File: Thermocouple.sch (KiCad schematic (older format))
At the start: 25 parts, among them P2 CONN_3X2, P3 CONN_2, U2 MCP3901, U3 LMT84, U4 OPA4170

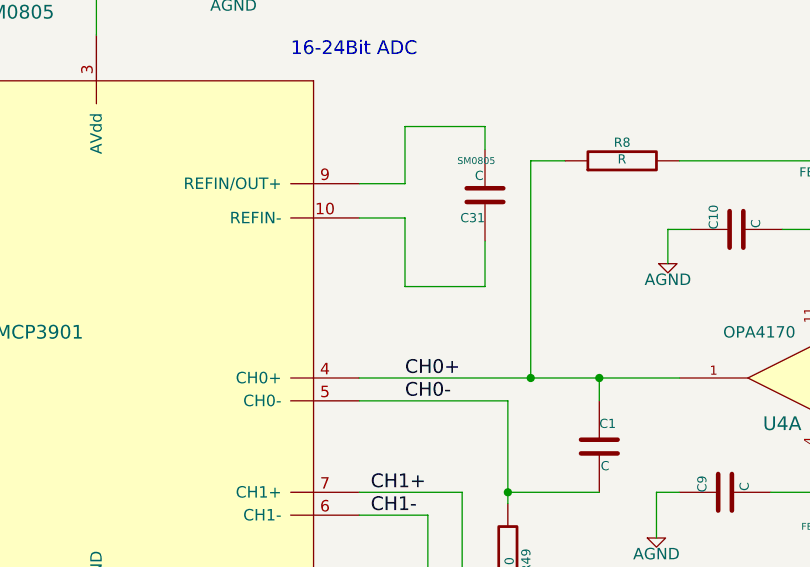
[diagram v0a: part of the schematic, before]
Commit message: Layout Work Session 15 Output
Silkscreen
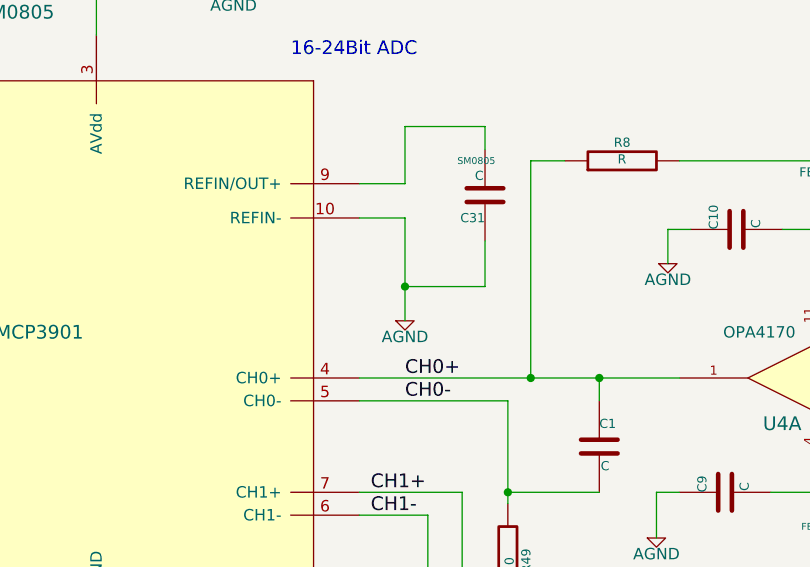
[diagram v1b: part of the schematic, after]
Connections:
- net AGND: now also C31.1, U2.10 (REFIN-)
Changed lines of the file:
@@
-EESchema Schematic File Version 2  date 11/24/2013 3:13:43 PM
+EESchema Schematic File Version 2  date 11/24/2013 8:21:44 PM
 LIBS:power
 LIBS:device
@@
 Connection ~ 4800 6800
 $Comp
-L +5V #PWR10
+L +5V #PWR01
 U 1 1 5257A1D1
 P 5600 5000
-F 0 "#PWR10" H 5600 5090 20  0001 C CNN
+F 0 "#PWR01" H 5600 5090 20  0001 C CNN
 F 1 "+5V" H 5600 5090 30  0000 C CNN
 F 2 "~" H 5600 5000 60  0000 C CNN
@@
 	6050 3800 6250 3800
 $Comp
-L +5V #PWR11
+L +5V #PWR02
 U 1 1 5257A5A4
 P 5600 5000
-F 0 "#PWR11" H 5600 5090 20  0001 C CNN
+F 0 "#PWR02" H 5600 5090 20  0001 C CNN
 F 1 "+5V" H 5600 5090 30  0000 C CNN
 F 2 "~" H 5600 5000 60  0000 C CNN
@@
 $EndComp
 $Comp
-L +5V #PWR3
+L +5V #PWR03
 U 1 1 5257A5AA
 P 3100 1300
-F 0 "#PWR3" H 3100 1390 20  0001 C CNN
+F 0 "#PWR03" H 3100 1390 20  0001 C CNN
 F 1 "+5V" H 3100 1390 30  0000 C CNN
 F 2 "~" H 3100 1300 60  0000 C CNN
@@
 $EndComp
 $Comp
-L FE_V+ #PWR13
+L FE_V+ #PWR04
 U 1 1 526E01E1
 P 6250 3850
-F 0 "#PWR13" H 6250 3950 30  0001 C CNN
+F 0 "#PWR04" H 6250 3950 30  0001 C CNN
 F 1 "FE_V+" H 6250 3950 30  0000 C CNN
 F 2 "~" H 6250 3850 60  0000 C CNN
@@
 $EndComp
 $Comp
-L FE_V+ #PWR17
+L FE_V+ #PWR05
 U 1 1 526E01F1
 P 9000 5000
-F 0 "#PWR17" H 9000 5100 30  0001 C CNN
+F 0 "#PWR05" H 9000 5100 30  0001 C CNN
 F 1 "FE_V+" H 9000 5100 30  0000 C CNN
 F 2 "~" H 9000 5000 60  0000 C CNN
@@
 $EndComp
 $Comp
-L FE_V+ #PWR14
+L FE_V+ #PWR06
 U 1 1 526E020D
 P 9000 1850
-F 0 "#PWR14" H 9000 1950 30  0001 C CNN
+F 0 "#PWR06" H 9000 1950 30  0001 C CNN
 F 1 "FE_V+" H 9000 1950 30  0000 C CNN
 F 2 "~" H 9000 1850 60  0000 C CNN
@@
 $EndComp
 $Comp
-L AGND #PWR4
+L AGND #PWR07
 U 1 1 527EEF67
 P 3100 4850
-F 0 "#PWR4" H 3100 4850 40  0001 C CNN
+F 0 "#PWR07" H 3100 4850 40  0001 C CNN
 F 1 "AGND" H 3100 4780 50  0000 C CNN
 F 2 "~" H 3100 4850 60  0000 C CNN
@@
 $EndComp
 $Comp
-L AGND #PWR2
+L AGND #PWR08
 U 1 1 527EEF6D
 P 2300 4850
-F 0 "#PWR2" H 2300 4850 40  0001 C CNN
+F 0 "#PWR08" H 2300 4850 40  0001 C CNN
 F 1 "AGND" H 2300 4780 50  0000 C CNN
 F 2 "~" H 2300 4850 60  0000 C CNN
@@
 $EndComp
 $Comp
-L AGND #PWR1
+L AGND #PWR09
 U 1 1 527EEF73
 P 1750 1650
-F 0 "#PWR1" H 1750 1650 40  0001 C CNN
+F 0 "#PWR09" H 1750 1650 40  0001 C CNN
 F 1 "AGND" H 1750 1580 50  0000 C CNN
 F 2 "~" H 1750 1650 60  0000 C CNN
@@
 $EndComp
 $Comp
-L AGND #PWR5
+L AGND #PWR010
 U 1 1 527EEF79
 P 3700 1600
-F 0 "#PWR5" H 3700 1600 40  0001 C CNN
+F 0 "#PWR010" H 3700 1600 40  0001 C CNN
 F 1 "AGND" H 3700 1530 50  0000 C CNN
 F 2 "~" H 3700 1600 60  0000 C CNN
@@
 $EndComp
 $Comp
-L AGND #PWR9
+L AGND #PWR011
 U 1 1 527EEF7F
 P 5600 2800
-F 0 "#PWR9" H 5600 2800 40  0001 C CNN
+F 0 "#PWR011" H 5600 2800 40  0001 C CNN
 F 1 "AGND" H 5600 2730 50  0000 C CNN
 F 2 "~" H 5600 2800 60  0000 C CNN
@@
 $EndComp
 $Comp
-L AGND #PWR8
+L AGND #PWR012
 U 1 1 527EEF85
 P 5550 4000
-F 0 "#PWR8" H 5550 4000 40  0001 C CNN
+F 0 "#PWR012" H 5550 4000 40  0001 C CNN
 F 1 "AGND" H 5550 3930 50  0000 C CNN
 F 2 "~" H 5550 4000 60  0000 C CNN
@@
 $EndComp
 $Comp
-L AGND #PWR7
+L AGND #PWR013
 U 1 1 527EEF8B
 P 4900 4700
-F 0 "#PWR7" H 4900 4700 40  0001 C CNN
+F 0 "#PWR013" H 4900 4700 40  0001 C CNN
 F 1 "AGND" H 4900 4630 50  0000 C CNN
 F 2 "~" H 4900 4700 60  0000 C CNN
@@
 $EndComp
 $Comp
-L AGND #PWR6
+L AGND #PWR014
 U 1 1 527EEF91
 P 4800 6900
-F 0 "#PWR6" H 4800 6900 40  0001 C CNN
+F 0 "#PWR014" H 4800 6900 40  0001 C CNN
 F 1 "AGND" H 4800 6830 50  0000 C CNN
 F 2 "~" H 4800 6900 60  0000 C CNN
@@
 	4450 2200 4450 2450
 Wire Wire Line
-	4450 2600 4450 2900
+	4450 2600 4450 3050
 Wire Wire Line
 	4450 2900 4800 2900
 Wire Wire Line
 	4800 2900 4800 2700
+$Comp
+L AGND #PWR015
+U 1 1 529271FF
+P 4450 3050
+F 0 "#PWR015" H 4450 3050 40  0001 C CNN
+F 1 "AGND" H 4450 2980 50  0000 C CNN
+F 2 "~" H 4450 3050 60  0000 C CNN
+F 3 "~" H 4450 3050 60  0000 C CNN
+	1    4450 3050
+	1    0    0    -1
+$EndComp
+Connection ~ 4450 2900
 $EndSCHEMATC

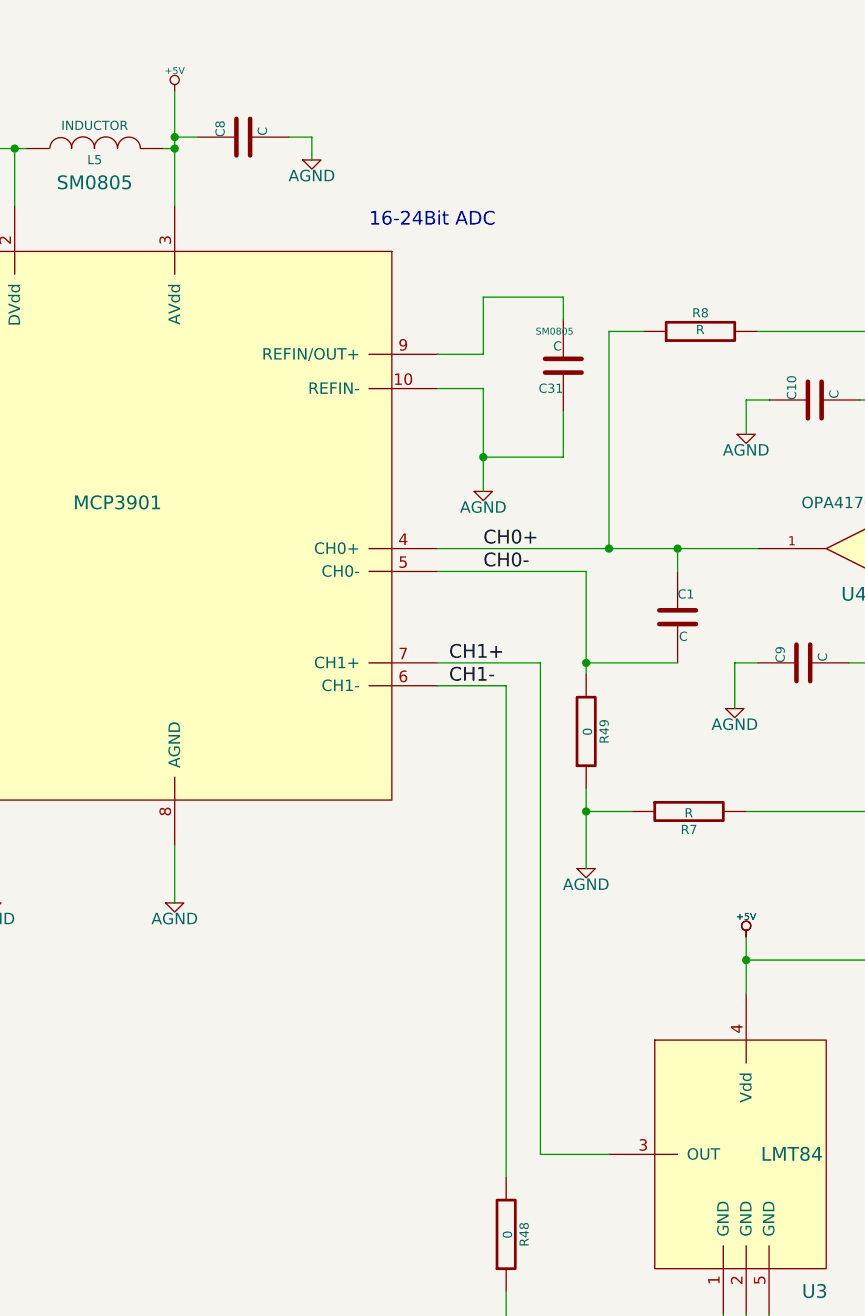
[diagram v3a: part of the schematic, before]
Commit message: Layout Work Session 18 Output
Added test points, changed a bunch of silk screen, added another
mounting hole and added a placeholder for the final commit number of the
board being sent to fab.
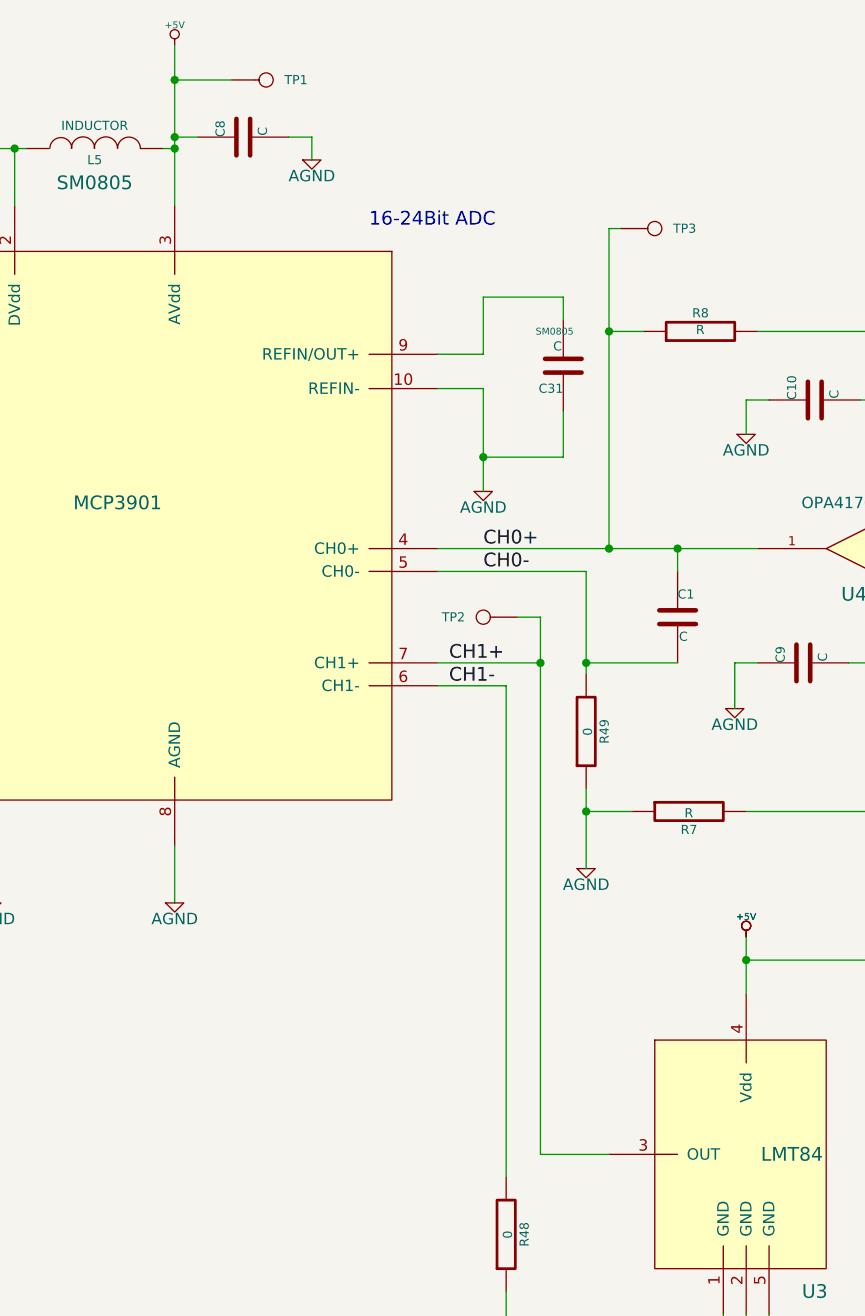
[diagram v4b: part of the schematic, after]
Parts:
- added TP1: 5V, symbol CONN_1
- added TP2: CH1, symbol CONN_1
- added TP3: CH0, symbol CONN_1
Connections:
- net +5V: now also TP1.1
- net CH0+: now also TP3.1
- net CH1+: now also TP2.1
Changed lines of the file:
@@
-EESchema Schematic File Version 2  date 12/3/2013 1:00:45 AM
+EESchema Schematic File Version 2  date 12/18/2013 11:27:15 PM
 LIBS:power
 LIBS:device
@@
 Sheet 2 9
 Title ""
-Date "3 dec 2013"
+Date "19 dec 2013"
 Rev ""
 Comp ""
@@
 	5150 2350 5000 2350
 Wire Wire Line
-	5000 2350 5000 3300
+	5000 1900 5000 3300
 Wire Wire Line
 	4250 3300 5650 3300
@@
 $EndComp
 Wire Wire Line
-	5000 5950 4700 5950
-Wire Wire Line
-	4700 5950 4700 3800
+	4700 5950 5000 5950
+Wire Wire Line
+	4700 3600 4700 5950
 Wire Wire Line
 	4700 3800 4250 3800
@@
 L +5V #PWR3
 U 1 1 5257A5AA
-P 3100 1300
-F 0 "#PWR3" H 3100 1390 20  0001 C CNN
-F 1 "+5V" H 3100 1390 30  0000 C CNN
-F 2 "~" H 3100 1300 60  0000 C CNN
-F 3 "~" H 3100 1300 60  0000 C CNN
-	1    3100 1300
-	1    0    0    -1
-$EndComp
-Wire Wire Line
-	3100 1300 3100 1800
+P 3100 1100
+F 0 "#PWR3" H 3100 1190 20  0001 C CNN
+F 1 "+5V" H 3100 1190 30  0000 C CNN
+F 2 "~" H 3100 1100 60  0000 C CNN
+F 3 "~" H 3100 1100 60  0000 C CNN
+	1    3100 1100
+	1    0    0    -1
+$EndComp
+Wire Wire Line
+	3100 1100 3100 1800
 Wire Wire Line
 	4450 2600 4250 2600
@@
 $EndComp
 Connection ~ 4450 2900
+$Comp
+L CONN_1 TP3
+U 1 1 52B27F2B
+P 5200 1900
+F 0 "TP3" H 5280 1900 40  0000 L CNN
+F 1 "CH0" H 5200 1955 30  0001 C CNN
+F 2 "" H 5200 1900 60  0000 C CNN
+F 3 "" H 5200 1900 60  0000 C CNN
+	1    5200 1900
+	1    0    0    -1
+$EndComp
+Wire Wire Line
+	5050 1900 5000 1900
+Connection ~ 5000 2350
+$Comp
+L CONN_1 TP2
+U 1 1 52B27FD1
+P 4450 3600
+F 0 "TP2" H 4530 3600 40  0000 L CNN
+F 1 "CH1" H 4450 3655 30  0001 C CNN
+F 2 "" H 4450 3600 60  0000 C CNN
+F 3 "" H 4450 3600 60  0000 C CNN
+	1    4450 3600
+	-1   0    0    1
+$EndComp
+Wire Wire Line
+	4600 3600 4700 3600
+Connection ~ 4700 3800
+$Comp
+L CONN_1 TP1
+U 1 1 52B2A6E5
+P 3500 1250
+F 0 "TP1" H 3580 1250 40  0000 L CNN
+F 1 "5V" H 3500 1305 30  0001 C CNN
+F 2 "" H 3500 1250 60  0000 C CNN
+F 3 "" H 3500 1250 60  0000 C CNN
+	1    3500 1250
+	1    0    0    -1
+$EndComp
+Wire Wire Line
+	3100 1250 3350 1250
+Connection ~ 3100 1250
 $EndSCHEMATC
